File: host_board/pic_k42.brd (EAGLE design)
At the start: 54.6 x 73.7 mm, 53 parts, among them IC1 PIC18F57K42-E_PT, IC2 REF3440IDBVR, IC3 MAX232, IC4 ILAMP, K1 G6K-2P, Q1 ASF1, X1 RX-2, X2 TX-2, X3 RESETJMP, X5 PORTA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

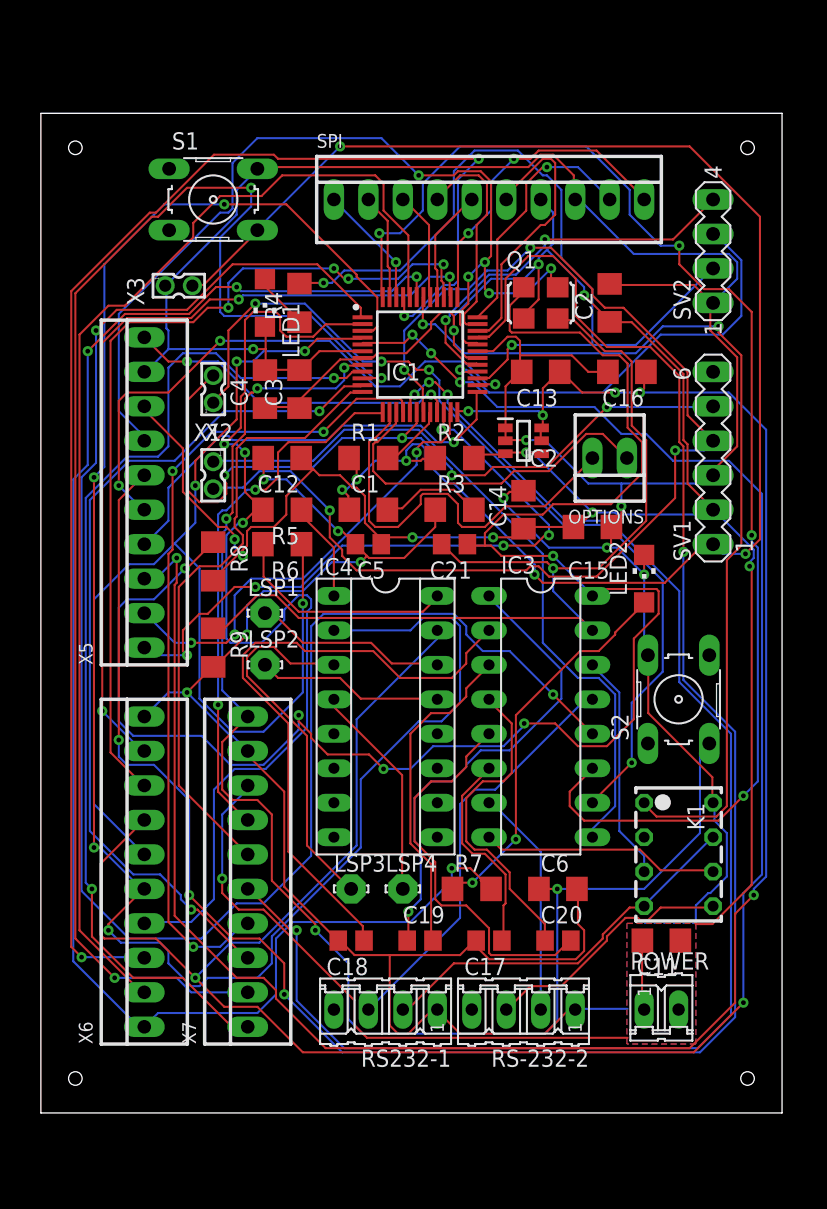
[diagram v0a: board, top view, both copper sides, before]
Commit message: update board to 1.2 spec
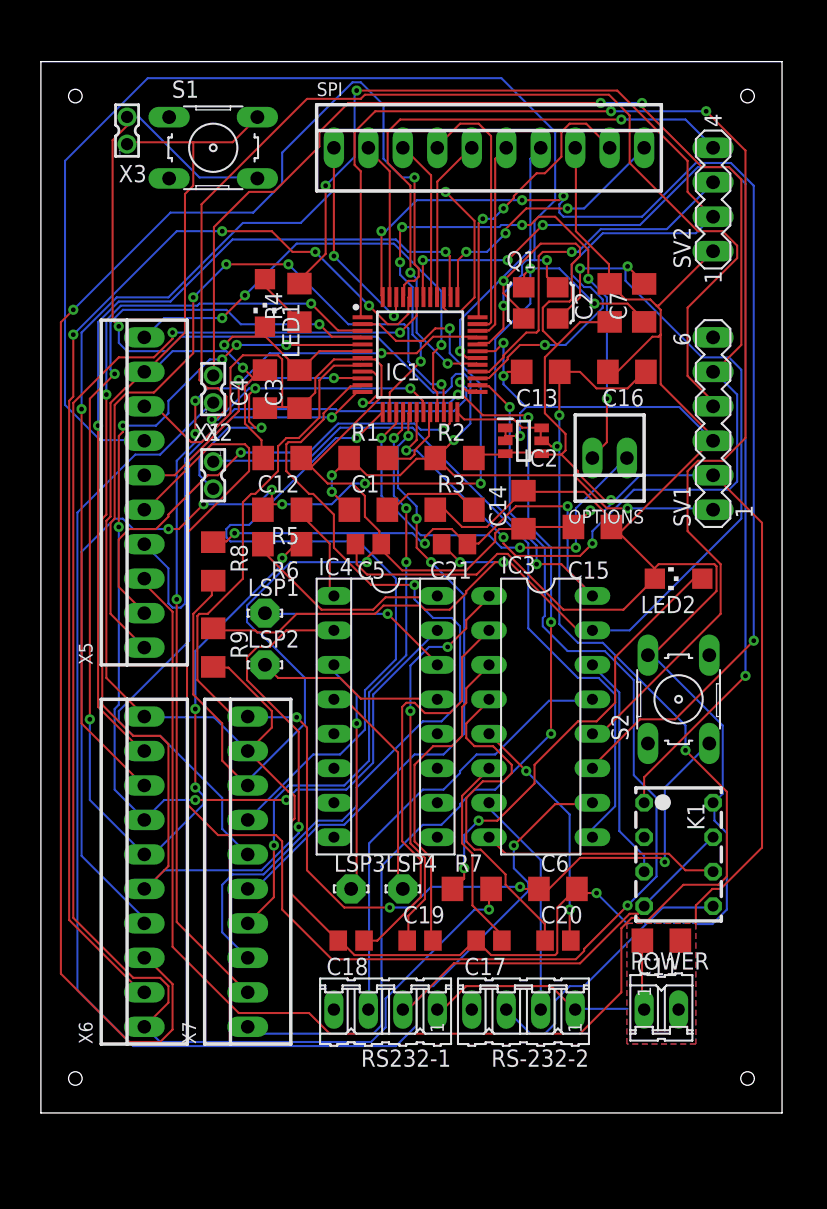
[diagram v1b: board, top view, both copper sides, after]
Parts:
- added C7: 0.1, rcl:C1206
- moved X3 12.0 mm to (30.5, 67.3), turned to 0 degrees
- moved S1 3.81 mm to (36.8, 66.0)
- moved SPI 3.81 mm to (57.1, 66.0)
- moved SV2 3.81 mm to (73.7, 62.2)
- moved LED2 2.54 mm to (71.1, 34.3), turned to 90 degrees
- moved SV1 2.54 mm to (73.7, 45.7)
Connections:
- net GND: now also C7.2
- net VCC: now also C7.1
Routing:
- net N$40: track 155.8 -> 30.2 mm, vias 4 -> 2
- net N$49: track 169.2 -> 81.2 mm, vias 5 -> 7
- net N$35: track 42.6 -> 126.7 mm, vias 3 -> 2
- net N$57: track 105.4 -> 46.8 mm, vias 4 -> 3
- net N$7: track 57.2 -> 114.5 mm, vias 4 -> 5
- net VCC: track 126.2 -> 77.3 mm, vias 5 -> 6
- net N$54: track 103.5 -> 59.4 mm, vias 3 -> 4
- net N$47: track 137.1 -> 101.1 mm, vias 4 -> 3
- net N$22: track 66.4 -> 100.2 mm, vias 4 -> 1
- net N$18: track 128.3 -> 95.6 mm
- net VSS: track 309.7 -> 335.6 mm, vias 11 -> 6
- net N$6: track 88.4 -> 111.1 mm
- net N$43: track 109.5 -> 90.0 mm, vias 5 -> 4
- net N$1: track 117.6 -> 99.4 mm, vias 6 -> 5
- net N$25: track 28.5 -> 46.4 mm, vias 2 -> 3
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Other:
- board size 54.6 x 73.7 mm -> 54.6 x 77.5 mm
- board text added: "1.2"
- board text removed: "1.1"

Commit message: update
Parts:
- removed R3: 0, rcl:R1206
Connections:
- removed net N$3: C1.2, R3.2
- net VSS: now also C1.2; no longer R3.1
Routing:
- net N$36: track 43.0 -> 141.1 mm, vias 1 -> 5
- net VSS: track 335.6 -> 396.6 mm, vias 6 -> 5
- net N$35: track 126.7 -> 75.5 mm, vias 2 -> 6
- net N$45: track 114.6 -> 63.8 mm
- net N$6: track 111.1 -> 61.9 mm
- net N$7: track 114.5 -> 69.4 mm, vias 5 -> 3
- net N$39: track 35.5 -> 68.9 mm, vias 3 -> 0
- net N$40: track 30.2 -> 63.3 mm, vias 2 -> 1
- net N$18: track 95.6 -> 62.8 mm
- net N$43: track 90.0 -> 122.7 mm, vias 4 -> 3
- net N$53: track 79.7 -> 110.2 mm, vias 5 -> 2
- net N$56: track 45.6 -> 68.5 mm, vias 4 -> 3
- net N$49: track 81.2 -> 103.7 mm, vias 7 -> 3
- net VDD: track 228.2 -> 246.8 mm, vias 5 -> 12
- net N$46: track 84.2 -> 100.0 mm, vias 7 -> 2
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
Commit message: update
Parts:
- removed LSP1, LSP2, LSP3, LSP4: LSP10, solpad:LSP10
- removed OPTIONS: 22-23-2021, con-molex:22-23-2021
- added C9: 0.1, rcl:C1206
- added LED3: DBLED, led:CHIPLED_1206
- added R10, R11, R3: 220, rcl:R1206
- IC4: device ic-package:SOCKET-16 -> ic-package:SOCKET-08
- moved K1 22.9 mm to (48.3, 14.0), turned to 0 degrees
- moved LED2 6.35 mm to (71.1, 27.9), turned to 180 degrees
- moved S2 6.35 mm to (71.1, 19.1)
- moved IC4 5.08 mm to (49.5, 29.2)
- moved C15 2.84 mm to (67.3, 39.4)
- moved C6 2.54 mm to (64.8, 11.4)
- moved R7 2.54 mm to (58.4, 11.4)
- moved SV1 2.54 mm to (73.7, 43.2)
- moved C14 1.27 mm to (61.0, 39.4), turned to 180 degrees
- moved IC2 1.27 mm to (61.0, 44.5)
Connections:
- removed net N$67: IC4.3, LSP3.MP
- removed net N$68: IC4.4, LSP4.MP
- new net N$17: IC4.8, R6.2
- net GND: now also C9.2
- net N$25: now also R11.2
- net N$49: now also IC4.7; no longer IC4.15
- net N$55: now also IC4.5, R3.2; no longer IC4.14, LSP1.MP
- net N$58: now also R10.2
- net N$59: now also IC4.3
- net N$60: now also IC4.6; no longer OPTIONS.1
- net N$61: now also R3.1; no longer OPTIONS.2
- net N$63: now also IC4.4, R10.1; no longer IC4.16, R6.2
- net N$65: now also LED3.A, R11.1; no longer IC4.13, LSP2.MP
- net VCC: now also C9.1, Q1.1
- net VDD: no longer Q1.1
- net VSS: now also LED3.C
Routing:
- net N$18: track 62.8 -> 134.5 mm, vias 2 -> 4
- net N$45: track 63.8 -> 128.1 mm, vias 2 -> 3
- net N$22: track 100.6 -> 47.7 mm, vias 5 -> 3
- net N$54: track 55.2 -> 107.6 mm, vias 3 -> 4
- net VSS: track 396.6 -> 346.8 mm, vias 5 -> 8
- net N$53: track 110.2 -> 63.3 mm, vias 2 -> 4
- net N$36: track 141.1 -> 103.7 mm, vias 5 -> 3
- net N$50: track 51.0 -> 87.7 mm, vias 2 -> 6
- net N$10: track 29.4 -> 64.3 mm, vias 1 -> 0
- net VDD: track 246.8 -> 212.7 mm, vias 12 -> 9
- net N$46: track 100.0 -> 131.5 mm, vias 2 -> 6
- net N$39: track 68.9 -> 39.9 mm, vias 0 -> 3
- net N$8: track 150.3 -> 121.8 mm, vias 4 -> 0
- net N$7: track 69.4 -> 96.0 mm, vias 3 -> 4
- net N$51: track 63.1 -> 87.8 mm
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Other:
- board text added: "1.3"
- board text removed: "1.2"

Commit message: new board
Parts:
- moved C11 4.02 mm to (71.1, 11.4)
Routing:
- net N$6: track 49.6 -> 122.0 mm, vias 3 -> 4
- net N$18: track 134.5 -> 86.6 mm, vias 4 -> 2
- net N$45: track 128.1 -> 81.3 mm, vias 3 -> 2
- net N$43: track 142.7 -> 98.0 mm, vias 2 -> 4
- net N$52: track 131.3 -> 172.9 mm, vias 4 -> 2
- net N$28: track 101.8 -> 61.4 mm, vias 4 -> 3
- net N$7: track 96.0 -> 58.8 mm, vias 4 -> 3
- net N$54: track 107.6 -> 71.4 mm, vias 4 -> 1
- net VDD: track 212.7 -> 245.1 mm, vias 9 -> 8
- net N$51: track 87.8 -> 59.6 mm, vias 2 -> 1
- net N$35: track 53.2 -> 29.4 mm, vias 3 -> 2
- net N$48: track 78.4 -> 101.8 mm, vias 7 -> 3
- net N$46: track 131.5 -> 109.7 mm, vias 6 -> 3
- net N$11: track 19.5 -> 40.9 mm
- net N$50: track 87.7 -> 66.5 mm, vias 6 -> 3
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
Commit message: update
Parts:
- added JMP2, JMP3: 0R-JUMPA, jump-0r-smd:A0R-JMP
- added SV3: USBH, con-lstb:MA03-1
- added X4: MINI-USB-UX60A-MB-5ST, con-hirose:UX60A-MB-5ST
- moved POWER 2.54 mm to (67.3, 2.54)
- moved C11 1.27 mm to (71.1, 12.7)
- moved LED2 1.27 mm to (71.1, 29.2), turned to 0 degrees
- moved S2 1.27 mm to (71.1, 20.3)
- turned R9 to 90 degrees
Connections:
- new net N$67: SV3.1, X4.4
- new net N$68: SV3.2, X4.3
- new net N$69: SV3.3, X4.2
- net GND: now also JMP2.2
- net VCC: now also JMP3.2
- net VDD: now also JMP3.1, X4.1
- net VSS: now also JMP2.1, X4.5
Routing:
- net N$52: track 172.9 -> 95.2 mm, vias 2 -> 6
- net N$67: track 0.00 -> 66.4 mm, vias 0 -> 1
- net N$47: track 117.7 -> 181.9 mm, vias 3 -> 2
- net N$8: track 126.8 -> 62.9 mm, vias 4 -> 7
- net N$36: track 114.9 -> 52.6 mm, vias 0 -> 4
- net N$39: track 24.4 -> 78.2 mm, vias 1 -> 3
- net N$69: track 0.00 -> 51.4 mm, vias 0 -> 1
- net N$68: track 0.00 -> 45.3 mm
- net N$1: track 86.8 -> 131.2 mm, vias 3 -> 6
- net N$49: track 102.3 -> 60.7 mm, vias 2 -> 4
- net N$22: track 55.7 -> 91.8 mm
- net N$9: track 62.3 -> 27.9 mm
- net N$6: track 122.0 -> 87.6 mm, vias 4 -> 3
- net VCC: track 81.9 -> 115.8 mm, vias 7 -> 5
- net N$60: track 53.7 -> 21.9 mm, vias 0 -> 1
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- removed copper zone on layer 1, net VDD
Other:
- board size 54.6 x 77.5 mm -> 55.9 x 85.1 mm
- board text added: "1.4"
- board text removed: "1.3"

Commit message: update
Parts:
- removed LED1: RUN, led:CHIPLED_1206
- removed LED2: MODE, led:CHIPLED_1206
- removed S1: RESETSW, switch-omron:B3F-10XX
- removed S2: MODESW, switch-omron:B3F-10XX
- added S3: MODE SW, SamacSys_Parts:B3W-9_1-LED
- added S4: RESET SW, SamacSys_Parts:B3W-9_1-LED
- moved SV3 45.6 mm to (71.1, 14.0), turned to 180 degrees
- moved C11 20.4 mm to (69.8, 33.0)
- moved X3 5.08 mm to (30.5, 62.2)
- moved R4 1.80 mm to (41.9, 53.3), turned to 180 degrees
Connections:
- net N$1: now also S4.4; no longer S1.4
- net N$21: now also S4.5; no longer LED1.A
- net N$43: now also S3.4; no longer S2.3
- net N$64: now also S3.5; no longer LED2.A
- net VSS: now also S3.2, S3.6, S4.2, S4.6; no longer LED1.C, LED2.C, S1.2, S2.2
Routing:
- net N$47: track 181.9 -> 71.7 mm, vias 2 -> 3
- net N$38: track 36.6 -> 131.5 mm, vias 1 -> 0
- net N$37: track 33.4 -> 125.8 mm, vias 3 -> 0
- net N$49: track 60.7 -> 128.2 mm, vias 4 -> 3
- net N$56: track 61.0 -> 0.00 mm, vias 2 -> 0
- net N$67: track 66.4 -> 10.7 mm, vias 1 -> 0
- net N$48: track 81.0 -> 136.3 mm, vias 5 -> 7
- net N$52: track 95.2 -> 149.6 mm, vias 6 -> 3
- net N$39: track 78.2 -> 24.8 mm, vias 3 -> 1
- net N$59: track 36.3 -> 78.4 mm, vias 1 -> 2
- net N$69: track 51.4 -> 11.4 mm, vias 1 -> 0
- net N$68: track 45.3 -> 10.6 mm
- net N$46: track 97.0 -> 64.5 mm, vias 4 -> 3
- net VSS: track 343.6 -> 311.3 mm, vias 7 -> 5
- net N$35: track 42.8 -> 74.3 mm, vias 3 -> 5
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- removed copper zone on layer 16, net VSS
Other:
- board size 55.9 x 85.1 mm -> 55.9 x 78.7 mm
- board text added: "/fred/Downloads/mchp.bmp"
- board text added: "1.5 FGB@MCHP"
- board text added: "these are the controllers you are looking for"
- board text removed: "1.4"

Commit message: update
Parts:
- moved LED3 7.87 mm to (73.4, 54.7)
- moved C9 6.34 mm to (67.3, 59.2)
- moved S3 0.71 mm to (72.6, 23.5)
- moved K1 0.14 mm to (48.2, 14.1)
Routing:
- net N$38: track 131.5 -> 32.8 mm, vias 0 -> 4
- net N$37: track 125.8 -> 36.9 mm, vias 0 -> 2
- net N$45: track 87.6 -> 161.9 mm, vias 2 -> 3
- net N$56: track 0.00 -> 64.9 mm, vias 0 -> 4
- net N$6: track 67.0 -> 127.3 mm
- net N$28: track 77.7 -> 129.6 mm, vias 4 -> 3
- net N$43: track 94.3 -> 141.7 mm, vias 4 -> 2
- net N$44: track 93.3 -> 140.6 mm, vias 0 -> 2
- net N$7: track 49.3 -> 93.3 mm, vias 3 -> 2
- net N$59: track 78.4 -> 38.4 mm, vias 2 -> 1
- net N$46: track 64.5 -> 96.3 mm, vias 3 -> 2
- net N$49: track 128.2 -> 99.7 mm, vias 3 -> 2
- net N$47: track 71.7 -> 99.4 mm
- net N$48: track 136.3 -> 109.6 mm, vias 7 -> 3
- net N$19: track 55.9 -> 81.6 mm, vias 0 -> 2
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
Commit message: up
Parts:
- added TP1, TP2: TPB1,27, testpad:B1,27
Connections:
- net VDD: now also TP2.TP
- net VSS: now also TP1.TP
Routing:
- net VDD: track 225.2 -> 230.4 mm
- net VSS: track 320.8 -> 323.5 mm
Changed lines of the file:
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@@
 <?xml version="1.0" encoding="utf-8"?>
 <!DOCTYPE eagle SYSTEM "eagle.dtd">
-<eagle version="9.4.0">
+<eagle version="9.5.0">
 <drawing>
 <settings>
@@
 <attribute name="VALUE" x="36.423009375" y="67.2667" size="1.27" layer="27" align="center"/>
 </element>
+<element name="TP1" library="testpad" library_urn="urn:adsk.eagle:library:385" package="B1,27" package3d_urn="urn:adsk.eagle:package:27944/2" value="TPB1,27" x="76.8858" y="11.5316" smashed="yes">
+<attribute name="NAME" x="76.2508" y="12.5476" size="1.27" layer="25" ratio="10"/>
+<attribute name="POPULARITY" value="19" x="76.8858" y="11.5316" size="1.778" layer="27" display="off"/>
+<attribute name="TP_SIGNAL_NAME" value="" x="76.8858" y="11.5316" size="1.778" layer="27" display="off"/>
+<attribute name="VALUE" x="76.2508" y="10.7696" size="0.0254" layer="27"/>
+</element>
+<element name="TP2" library="testpad" library_urn="urn:adsk.eagle:library:385" package="B1,27" package3d_urn="urn:adsk.eagle:package:27944/2" value="TPB1,27" x="67.2846" y="7.7216" smashed="yes">
+<attribute name="NAME" x="66.6496" y="8.7376" size="1.27" layer="25" ratio="10"/>
+<attribute name="POPULARITY" value="19" x="67.2846" y="7.7216" size="1.778" layer="27" display="off"/>
+<attribute name="TP_SIGNAL_NAME" value="" x="67.2846" y="7.7216" size="1.778" layer="27" display="off"/>
+<attribute name="VALUE" x="66.6496" y="6.9596" size="0.0254" layer="27"/>
+</element>
 </elements>
 <signals>
@@
 <via x="67.056" y="40.6908" extent="1-16" drill="0.35"/>
 <via x="59.7408" y="47.0916" extent="1-16" drill="0.35"/>
+<contactref element="TP2" pad="TP"/>
+<wire x1="67.3608" y1="5.334" x2="67.3608" y2="7.62" width="0.1524" layer="1"/>
+<wire x1="69.342" y1="3.3528" x2="67.3608" y2="5.334" width="0.1524" layer="1"/>
+<wire x1="67.3608" y1="7.62" x2="67.2846" y2="7.7216" width="0.1524" layer="1"/>
 </signal>
 <signal name="VSS">
@@
 <via x="64.77" y="54.7116" extent="1-16" drill="0.35"/>
 <via x="68.1228" y="31.5468" extent="1-16" drill="0.35"/>
+<contactref element="TP1" pad="TP"/>
+<wire x1="75.8952" y1="11.5824" x2="76.8096" y2="11.5824" width="0.1524" layer="1"/>
+<wire x1="74.676" y1="12.8016" x2="75.8952" y2="11.5824" width="0.1524" layer="1"/>
+<wire x1="76.8096" y1="11.5824" x2="76.8858" y2="11.5316" width="0.1524" layer="1"/>
 </signal>
 <signal name="N$6">
